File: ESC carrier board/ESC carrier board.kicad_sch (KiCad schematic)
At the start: 11 parts, among them J1 Conn_01x04_Pin, J3 Conn_01x04_Pin, J4 Conn_01x04_Pin, U1 ESC, U2 ESC, U3 ESC

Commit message: Partially cleaned up schematic
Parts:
- added J5: Conn_01x10_Pin, symbol Connector:Conn_01x10_Pin
- J2: footprint ESC carrier board test 1:MR60PW-M_X3 -> 2024-backplane:MR60PW-M_X3
- U1: footprint ESC carrier board test 1:ESC -> ESC:ESC
- U7: symbol Kelpie_Library:ESP32-S3-Pico -> Kelpie_Library:Raspberry-Pi-Pico
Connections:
- net sGP8: now also J1.4 (Pin_4), U1.S, U7.11 (GP8); no longer U3.S, U7.32 (GP8)
- net sg: now also J1.1 (Pin_1); no longer J1.4 (Pin_4)
- net at J4.4 (Pin_4): now also U7.27 (GP21); no longer U7.29 (GP6)
- net at J3.2 (Pin_2): now also U7.4 (GP2); no longer U7.7 (GP16)
- net at J3.3 (Pin_3): now also U7.2 (GP1); no longer U7.5 (GP14)
- net at J3.4 (Pin_4): now also U7.1 (GP0); no longer U7.2 (GP12)
- net sGP7: now reaches U7.10 (GP7)
- net sGP7: now also J1.3 (Pin_3), U2.S
- net sGP6: now reaches U7.9 (GP6)
- net sGP6: now also J1.2 (Pin_2), U3.S
- removed net sGP10: J1.1 (Pin_1), J1.2 (Pin_2), U2.S, U7.35 (GP10)
- removed net signalGP39: J1.3 (Pin_3), U1.S
- no-connect marks 0 -> 2
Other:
- moved on the sheet: J1, J2A, J2B, J2C, J4, U1, U2, U3, U4, U5, U6, U7

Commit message: Minor changes to schematic
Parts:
- removed J5: Conn_01x10_Pin, symbol Connector:Conn_01x10_Pin
- added J5: ~, 2024-backplane:CardEdge_2x10, symbol 2024-backplane:Backplane_Card_Edge
- added JP1, JP2: Jumper_2_Bridged, symbol Jumper:Jumper_2_Bridged
- J2: footprint ESC carrier board test 1:MR60PW-M_X3 -> 2024-backplane:MR60PW-M_X3
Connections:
- net at J4.2 (Pin_2): now also U7.21 (GP16); no longer U7.25 (GP19)
- net at J4.3 (Pin_3): now also U7.22 (GP17); no longer U7.26 (GP20)
- net at J4.4 (Pin_4): now also U7.24 (GP18); no longer U7.27 (GP21)
- net at J3.2 (Pin_2): now also U7.7 (GP5); no longer U7.4 (GP2)
- net at J3.3 (Pin_3): now also U7.6 (GP4); no longer U7.2 (GP1)
- net at J3.4 (Pin_4): now also U7.5 (GP3); no longer U7.1 (GP0)
- net SDA1: now reaches U7.31 (GP26)
- net SDA1: now also JP2.2 (B)
- net SCL1: now reaches U7.32 (GP27)
- net SCL1: now also JP1.2 (B)
- new net: J5.8 (TX2/SDA2), JP2.1 (A)
- new net: J5.9 (RX2/SCL2), JP1.1 (A)
- new net RX0: U7.2 (GP1)
- new net SCL0: U7.27 (GP21)
- new net SDA0: U7.26 (GP20)
- new net TX0: U7.1 (GP0)
- new net sGND: J5.1 (sGND), J5.10 (sGND), J5.4 (sGND), J5.7 (sGND)
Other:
- moved on the sheet: J4

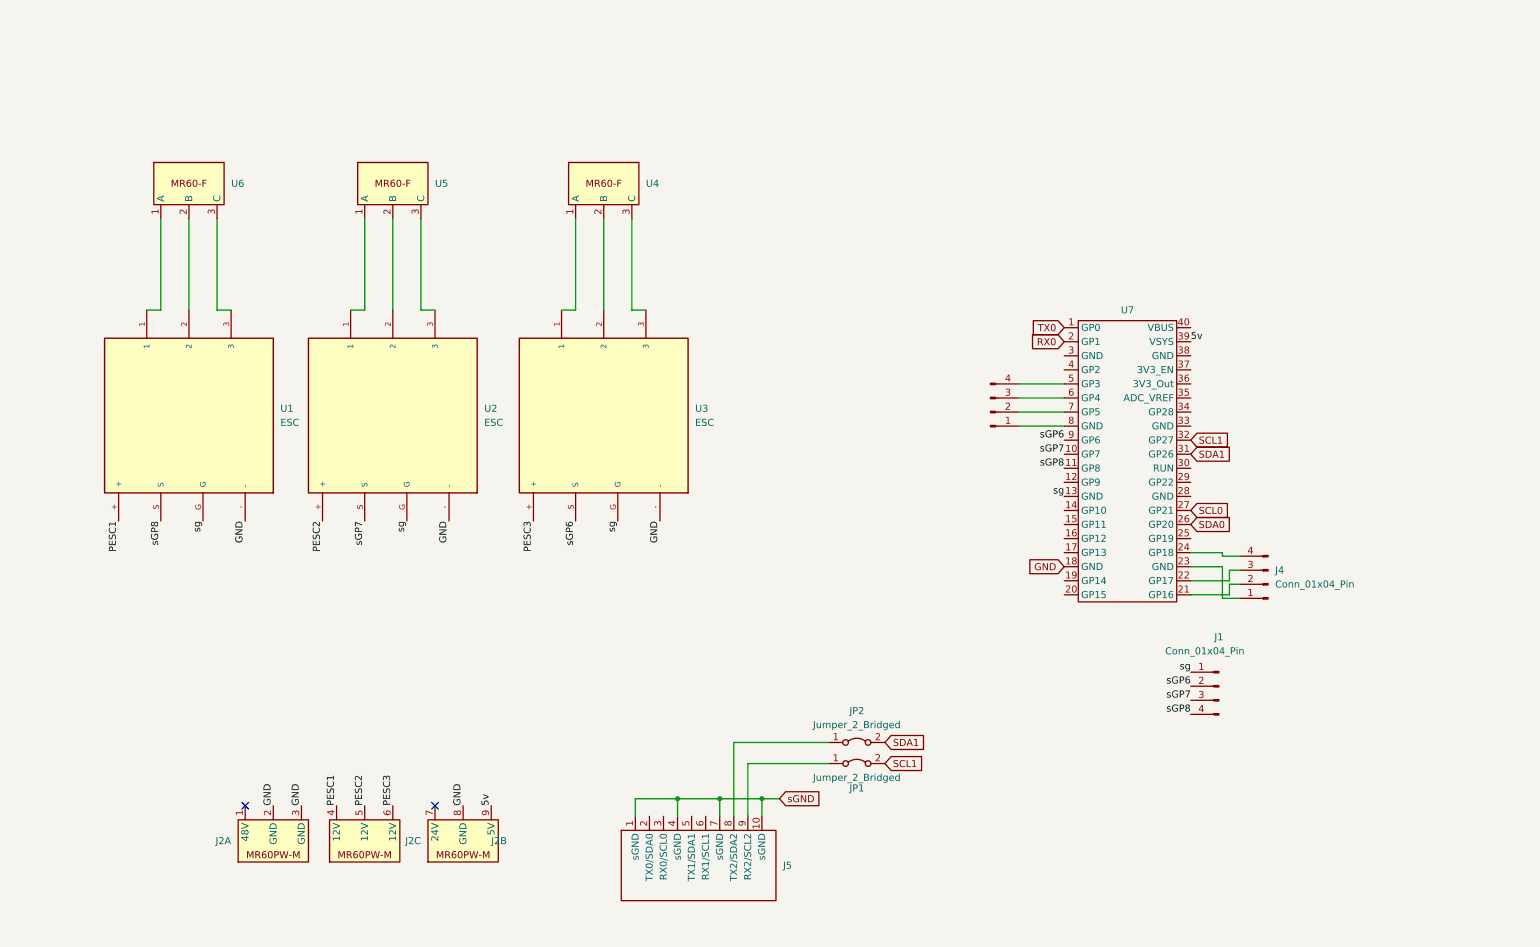
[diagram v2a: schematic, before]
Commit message: Updated Schematic and components
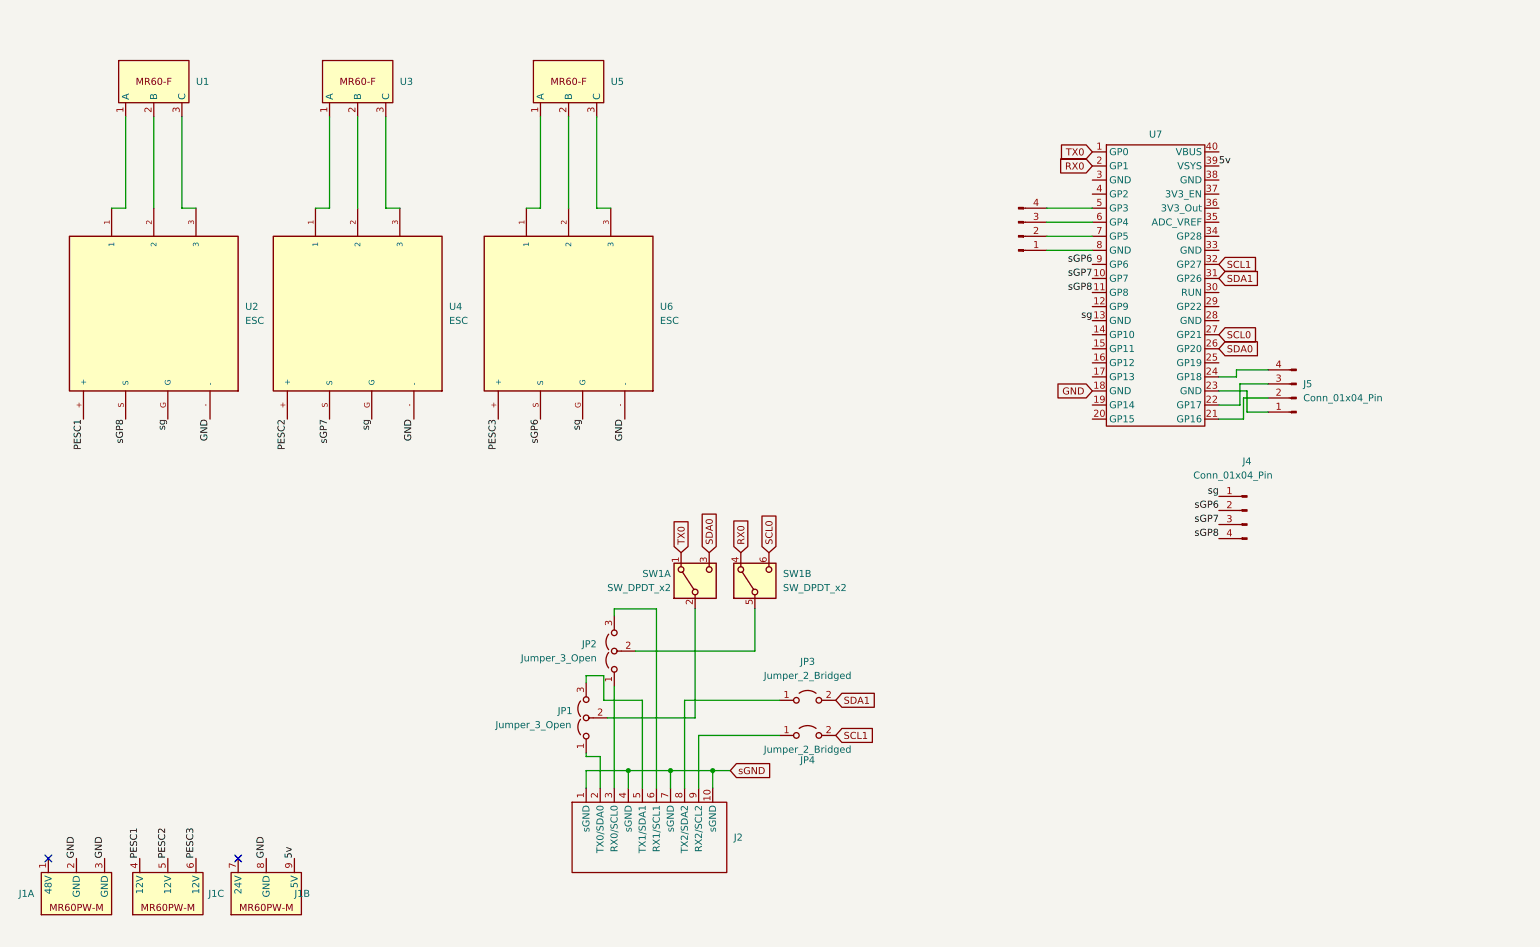
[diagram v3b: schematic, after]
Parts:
- added JP1, JP2: Jumper_3_Open, Jumper:SolderJumper-3_P1.3mm_Open_RoundedPad1.0x1.5mm, symbol Jumper:Jumper_3_Open
- added SW1: SW_DPDT_x2, Kelpie_Default:CUI-Switch-SMD, symbol Switch:SW_DPDT_x2
- JP3: renamed from JP2; footprint (none) -> Jumper:SolderJumper-2_P1.3mm_Open_RoundedPad1.0x1.5mm; symbol Jumper:Jumper_2_Bridged -> Jumper:Jumper_2_Open
- JP4: renamed from JP1; footprint (none) -> Jumper:SolderJumper-2_P1.3mm_Open_RoundedPad1.0x1.5mm; symbol Jumper:Jumper_2_Bridged -> Jumper:Jumper_2_Open
- U2: renamed from U1; footprint ESC:ESC -> ESC-carrier:ESC
- U4: renamed from U2; footprint ESC carrier board test 1:ESC -> ESC-carrier:ESC
- U6: renamed from U3; footprint ESC carrier board test 1:ESC -> ESC-carrier:ESC
- renumbered J2 to J1, J5 to J2, J1 to J4, J4 to J5, U6 to U1, U5 to U3, U4 to U5
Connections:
- net RX0: now also SW1.4 (A)
- net SCL0: now also SW1.6 (C)
- net SDA0: now also SW1.3 (C)
- net TX0: now also SW1.1 (A)
- net at J2.2 (TX0/SDA0): now also JP1.1 (A)
- net at J2.3 (RX0/SCL0): now also JP2.1 (A)
- net at J2.5 (TX1/SDA1): now also JP1.3 (B)
- net at J2.6 (RX1/SCL1): now also JP2.3 (B)
- new net: JP2.2 (C), SW1.5 (B)
- new net: JP1.2 (C), SW1.2 (B)
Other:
- moved on the sheet: J1A, J1B, J1C, J2, J4, J5, JP3, JP4, U1, U2, U3, U4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

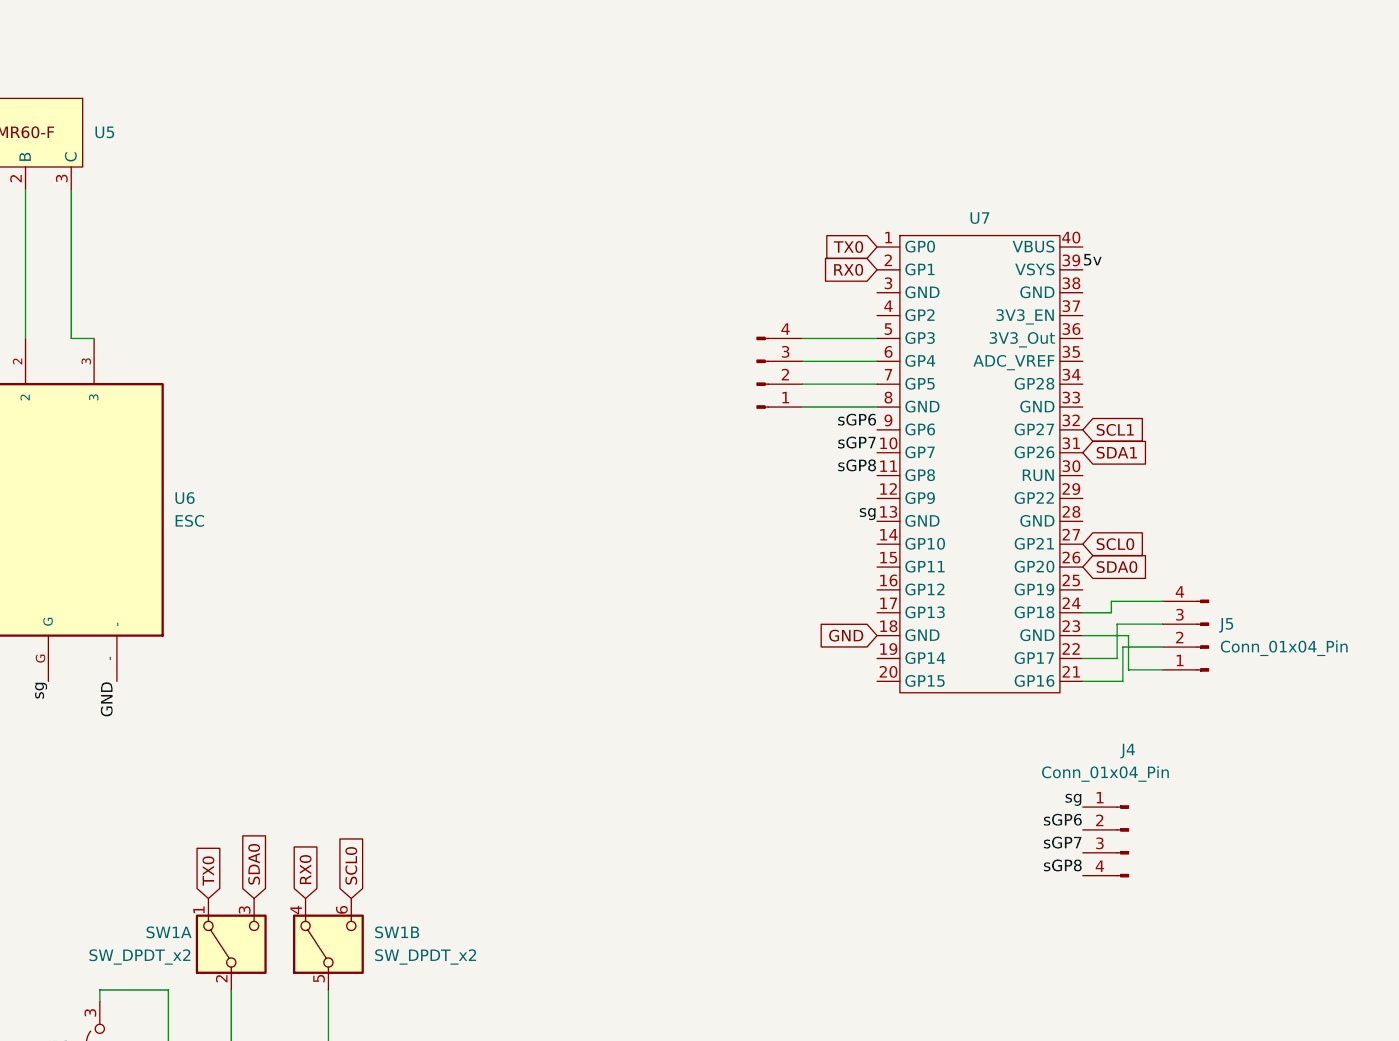
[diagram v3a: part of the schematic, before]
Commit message: esc carrier boards
updated carrier board pcb, it is not routed yet and some clarification as to what pins to connect to the card edge connector is still required.
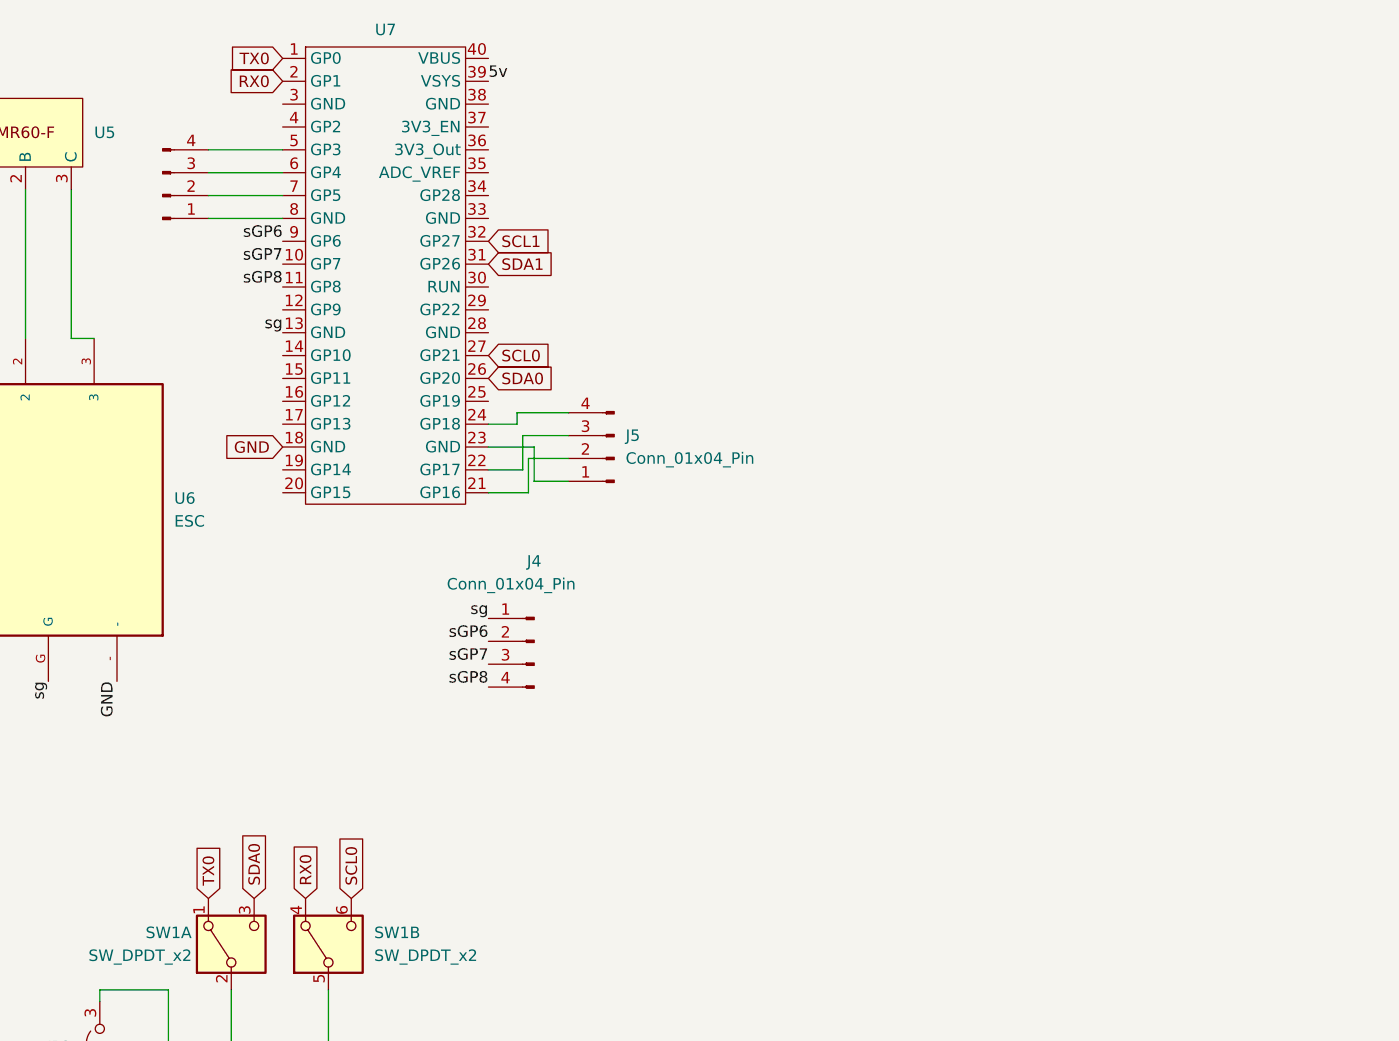
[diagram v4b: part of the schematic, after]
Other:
- moved on the sheet: J4, J5, U7
